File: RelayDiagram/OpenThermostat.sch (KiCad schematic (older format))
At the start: 90 parts, among them J1 Conn_01x08_Female, J2 Conn_01x15_Female, J3 Conn_01x15_Female, J4 Conn_01x09_Female, Q1 Q_NMOS_DGS, Q10 Q_NMOS_DGS, Q11 Q_NMOS_DGS, Q12 Q_NMOS_DGS, Q2 Q_NMOS_DGS, Q3 Q_NMOS_DGS, Q4 Q_NMOS_DGS, Q5 Q_NMOS_DGS, Q6 Q_NMOS_DGS, Q7 Q_NMOS_DGS, Q8 Q_NMOS_DGS, Q9 Q_NMOS_DGS, SW2 SW_Push, SW3 SW_Push, SW4 SW_Push, SW5 SW_Push, SW6 SW_Push, U1 PCF8574, U10 MB10S-13, U11 L7805CV, U2 LCD, U3 DHT11, U4 EE2-3TNU-L_DPDT_Relay, U5 EE2-3TNU-L_DPDT_Relay, U6 EE2-3TNU-L_DPDT_Relay, U7 EE2-3TNU-L_DPDT_Relay, U8 EE2-3TNU-L_DPDT_Relay, U9 EE2-3TNU-L_DPDT_Relay

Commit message: Major routing. Board should be nearly complete apart from review and minor changes.
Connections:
- wire segments 399 -> 463
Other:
- moved on the sheet: J4

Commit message: added mounting holes and power indicator LED
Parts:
- added D13: LED, Diodes_SMD:D_0805, symbol Device:LED
- added R46: 100, Resistors_SMD:R_0805, symbol Device:R
- C1: symbol solarcar-device:Capacitor_Unpolarized -> OpenThermostat-rescue:Capacitor_Unpolarized-solarcar-device
- J1: footprint Pin_Headers:Pin_Header_Angled_1x08_Pitch2.54mm -> Pin_Headers:Pin_Header_Angled_1x03_Pitch1.27mm
- J2: footprint Pin_Headers:Pin_Header_Straight_1x15_Pitch2.54mm -> Pin_Headers:Pin_Header_Straight_1x13_Pitch2.54mm_SMD_Pin1Right
- U10: symbol OpenThermostat-rescue:MB10S-13 -> OpenThermostat-rescue:MB10S-13-OpenThermostat-rescue
- U11: symbol OpenThermostat-rescue:L7805CV -> OpenThermostat-rescue:L7805CV-OpenThermostat-rescue
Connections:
- wire segments 463 -> 466
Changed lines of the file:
@@
 F 0 "J2" H 2900 2600 50  0000 L CNN
 F 1 "Conn_01x15_Female" H 2225 2525 50  0000 L CNN
-F 2 "Pin_Headers:Pin_Header_Straight_1x15_Pitch2.54mm" H 2950 3425 50  0001 C CNN
+F 2 "Pin_Headers:Pin_Header_Straight_1x13_Pitch2.54mm_SMD_Pin1Right" H 2950 3425 50  0001 C CNN
 F 3 "~" H 2950 3425 50  0001 C CNN
 	1    2950 3425
@@
 F 0 "J1" V 2100 655 50  0000 C CNN
 F 1 "Conn_01x08_Female" V 2009 655 50  0000 C CNN
-F 2 "Pin_Headers:Pin_Header_Angled_1x08_Pitch2.54mm" H 1935 725 50  0001 C CNN
+F 2 "Pin_Headers:Pin_Header_Angled_1x03_Pitch1.27mm" H 1935 725 50  0001 C CNN
 F 3 "~" H 1935 725 50  0001 C CNN
 	1    1935 725
@@
 $EndComp
 $Comp
-L OpenThermostat-rescue:MB10S-13 U10
+L OpenThermostat-rescue:MB10S-13-OpenThermostat-rescue U10
 U 1 1 5C64C7AA
 P 10975 2675
@@
 R
 $Comp
-L OpenThermostat-rescue:L7805CV U11
+L OpenThermostat-rescue:L7805CV-OpenThermostat-rescue U11
 U 1 1 5C651BD2
 P 10975 3425
@@
 $EndComp
 $Comp
-L solarcar-device:Capacitor_Unpolarized C1
+L OpenThermostat-rescue:Capacitor_Unpolarized-solarcar-device C1
 U 1 1 5C65344A
 P 11450 2675
@@
 Wire Wire Line
 	4725 3825 3950 3825
+$Comp
+L Device:LED D13
+U 1 1 5C7ACEAE
+P 2060 7800
+F 0 "D13" H 2052 7545 50  0000 C CNN
+F 1 "LED" H 2052 7636 50  0000 C CNN
+F 2 "Diodes_SMD:D_0805" H 2060 7800 50  0001 C CNN
+F 3 "~" H 2060 7800 50  0001 C CNN
+	1    2060 7800
+	-1   0    0    1
+$EndComp
+$Comp
+L Device:R R46
+U 1 1 5C7AD1B1
+P 2465 7800
+F 0 "R46" V 2340 7805 50  0000 C CNN
+F 1 "100" V 2465 7805 50  0000 C CNN
+F 2 "Resistors_SMD:R_0805" V 2395 7800 50  0001 C CNN
+F 3 "~" H 2465 7800 50  0001 C CNN
+	1    2465 7800
+	0    1    1    0
+$EndComp
+Wire Wire Line
+	2210 7800 2315 7800
+Wire Wire Line
+	2615 7800 2655 7800
+Wire Wire Line
+	1910 7800 1890 7800
+$Comp
+L power:+5V #PWR0101
+U 1 1 5C851227
+P 1890 7800
+F 0 "#PWR0101" H 1890 7650 50  0001 C CNN
+F 1 "+5V" V 1905 7928 50  0000 L CNN
+F 2 "" H 1890 7800 50  0001 C CNN
+F 3 "" H 1890 7800 50  0001 C CNN
+	1    1890 7800
+	0    -1   -1   0
+$EndComp
+$Comp
+L power:GND #PWR0102
+U 1 1 5C851537
+P 2655 7800
+F 0 "#PWR0102" H 2655 7550 50  0001 C CNN
+F 1 "GND" V 2660 7672 50  0000 R CNN
+F 2 "" H 2655 7800 50  0001 C CNN
+F 3 "" H 2655 7800 50  0001 C CNN
+	1    2655 7800
+	0    -1   -1   0
+$EndComp
 $EndSCHEMATC

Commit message: Changed to big boy header and added great logo
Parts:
- added C2, C3: 10uF, solarcar-device:Capacitor_0805, symbol OpenThermostat-rescue:Capacitor_Unpolarized-solarcar-device-OpenThermostat-resc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
- C1: symbol OpenThermostat-rescue:Capacitor_Unpolarized-solarcar-device -> OpenThermostat-rescue:Capacitor_Unpolarized-solarcar-device-OpenThermostat-rescue
- J4: footprint Pin_Headers:Pin_Header_Straight_1x09_Pitch2.54mm -> SeniorDesign:5mmPtichBlockHeader
- U10: symbol OpenThermostat-rescue:MB10S-13-OpenThermostat-rescue -> OpenThermostat-rescue:MB10S-13-OpenThermostat-rescue-OpenThermostat-rescue
- U11: symbol OpenThermostat-rescue:L7805CV-OpenThermostat-rescue -> OpenThermostat-rescue:L7805CV-OpenThermostat-rescue-OpenThermostat-rescue
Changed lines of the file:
@@
 F 0 "J4" H 10400 5900 50  0000 L CNN
 F 1 "Conn_01x09_Female" H 10400 5825 50  0000 L CNN
-F 2 "Pin_Headers:Pin_Header_Straight_1x09_Pitch2.54mm" H 10575 5325 50  0001 C CNN
+F 2 "SeniorDesign:5mmPtichBlockHeader" H 10575 5325 50  0001 C CNN
 F 3 "~" H 10575 5325 50  0001 C CNN
 	1    10575 5325
@@
 $EndComp
 $Comp
-L OpenThermostat-rescue:MB10S-13-OpenThermostat-rescue U10
+L OpenThermostat-rescue:MB10S-13-OpenThermostat-rescue-OpenThermostat-rescue U10
 U 1 1 5C64C7AA
 P 10975 2675
@@
 R
 $Comp
-L OpenThermostat-rescue:L7805CV-OpenThermostat-rescue U11
+L OpenThermostat-rescue:L7805CV-OpenThermostat-rescue-OpenThermostat-rescue U11
 U 1 1 5C651BD2
 P 10975 3425
@@
 $EndComp
 $Comp
-L OpenThermostat-rescue:Capacitor_Unpolarized-solarcar-device C1
+L OpenThermostat-rescue:Capacitor_Unpolarized-solarcar-device-OpenThermostat-rescue C1
 U 1 1 5C65344A
 P 11450 2675
@@
 	0    -1   -1   0
 $EndComp
+$Comp
+L OpenThermostat-rescue:Capacitor_Unpolarized-solarcar-device-OpenThermostat-rescue C3
+U 1 1 5C778E29
+P 3950 2575
+F 0 "C3" H 3975 2675 59  0000 L CNN
+F 1 "10uF" H 4000 2475 59  0000 L CNN
+F 2 "solarcar-device:Capacitor_0805" H 3050 3425 50  0001 C CNN
+F 3 "" H 3950 2575 50  0001 C CNN
+	1    3950 2575
+	1    0    0    -1
+$EndComp
+Connection ~ 3950 2725
+$Comp
+L power:GND #PWR0103
+U 1 1 5C7795E4
+P 3950 2425
+F 0 "#PWR0103" H 3950 2175 50  0001 C CNN
+F 1 "GND" H 3955 2252 50  0000 C CNN
+F 2 "" H 3950 2425 50  0001 C CNN
+F 3 "" H 3950 2425 50  0001 C CNN
+	1    3950 2425
+	0    1    1    0
+$EndComp
+$Comp
+L OpenThermostat-rescue:Capacitor_Unpolarized-solarcar-device-OpenThermostat-rescue C2
+U 1 1 5C77A8FC
+P 1635 4740
+F 0 "C2" H 1660 4840 59  0000 L CNN
+F 1 "10uF" H 1685 4640 59  0000 L CNN
+F 2 "solarcar-device:Capacitor_0805" H 735 5590 50  0001 C CNN
+F 3 "" H 1635 4740 50  0001 C CNN
+	1    1635 4740
+	1    0    0    -1
+$EndComp
+Connection ~ 1635 4890
+$Comp
+L power:GND #PWR0104
+U 1 1 5C77BDF8
+P 1635 4590
+F 0 "#PWR0104" H 1635 4340 50  0001 C CNN
+F 1 "GND" V 1640 4462 50  0000 R CNN
+F 2 "" H 1635 4590 50  0001 C CNN
+F 3 "" H 1635 4590 50  0001 C CNN
+	1    1635 4590
+	0    1    1    0
+$EndComp
 $EndSCHEMATC

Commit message: changed ports on micro controller to get input only ports connected to switches
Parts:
- C1, C2, C3: symbol OpenThermostat-rescue:Capacitor_Unpolarized-solarcar-device-OpenThermostat-rescue -> OpenThermostat-rescue:Capacitor_Unpolarized-solarcar-device-OpenThermostat-rescue-OpenThermostat-rescue
- U10: symbol OpenThermostat-rescue:MB10S-13-OpenThermostat-rescue-OpenThermostat-rescue -> OpenThermostat-rescue:MB10S-13-OpenThermostat-rescue-OpenThermostat-rescue-OpenThermostat-rescue
- U11: symbol OpenThermostat-rescue:L7805CV-OpenThermostat-rescue-OpenThermostat-rescue -> OpenThermostat-rescue:L7805CV-OpenThermostat-rescue-OpenThermostat-rescue-OpenThermostat-rescue
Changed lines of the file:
@@
 $EndComp
 $Comp
-L OpenThermostat-rescue:MB10S-13-OpenThermostat-rescue-OpenThermostat-rescue U10
+L OpenThermostat-rescue:MB10S-13-OpenThermostat-rescue-OpenThermostat-rescue-OpenThermostat-rescue U10
 U 1 1 5C64C7AA
 P 10975 2675
@@
 R
 $Comp
-L OpenThermostat-rescue:L7805CV-OpenThermostat-rescue-OpenThermostat-rescue U11
+L OpenThermostat-rescue:L7805CV-OpenThermostat-rescue-OpenThermostat-rescue-OpenThermostat-rescue U11
 U 1 1 5C651BD2
 P 10975 3425
@@
 $EndComp
 $Comp
-L OpenThermostat-rescue:Capacitor_Unpolarized-solarcar-device-OpenThermostat-rescue C1
+L OpenThermostat-rescue:Capacitor_Unpolarized-solarcar-device-OpenThermostat-rescue-OpenThermostat-rescue C1
 U 1 1 5C65344A
 P 11450 2675
@@
 	1655 3925 1655 4565
 Wire Wire Line
-	1655 4565 4110 4565
-Wire Wire Line
 	2750 4125 1735 4125
 Wire Wire Line
 	1735 4125 1735 4515
-Wire Wire Line
-	1735 4515 4225 4515
 Wire Wire Line
 	6375 900  6400 900
@@
 	6075 9950 4725 9950
 Wire Wire Line
-	4725 9950 4725 3825
-Wire Wire Line
 	6075 9125 4825 9125
-Wire Wire Line
-	4825 9125 4825 3725
 Wire Wire Line
 	6075 8325 4925 8325
@@
 Wire Wire Line
 	3990 4640 3990 6040
-Wire Wire Line
-	4110 4565 4110 6040
-Wire Wire Line
-	4225 4515 4225 6040
 Wire Wire Line
 	8400 8800 8425 8800
@@
 Wire Wire Line
 	4925 3625 3950 3625
-Wire Wire Line
-	4825 3725 3950 3725
-Wire Wire Line
-	4725 3825 3950 3825
 $Comp
 L Device:LED D13
@@
 $EndComp
 $Comp
-L OpenThermostat-rescue:Capacitor_Unpolarized-solarcar-device-OpenThermostat-rescue C3
+L OpenThermostat-rescue:Capacitor_Unpolarized-solarcar-device-OpenThermostat-rescue-OpenThermostat-rescue C3
 U 1 1 5C778E29
 P 3950 2575
@@
 $EndComp
 $Comp
-L OpenThermostat-rescue:Capacitor_Unpolarized-solarcar-device-OpenThermostat-rescue C2
+L OpenThermostat-rescue:Capacitor_Unpolarized-solarcar-device-OpenThermostat-rescue-OpenThermostat-rescue C2
 U 1 1 5C77A8FC
 P 1635 4740
@@
 	0    1    1    0
 $EndComp
+Wire Wire Line
+	4825 4515 4825 9125
+Wire Wire Line
+	1735 4515 4825 4515
+Wire Wire Line
+	4725 4565 4725 9950
+Wire Wire Line
+	1655 4565 4725 4565
+Wire Wire Line
+	4110 6040 4110 3825
+Wire Wire Line
+	4110 3825 3950 3825
+Wire Wire Line
+	3950 3725 4225 3725
+Wire Wire Line
+	4225 3725 4225 6040
 $EndSCHEMATC

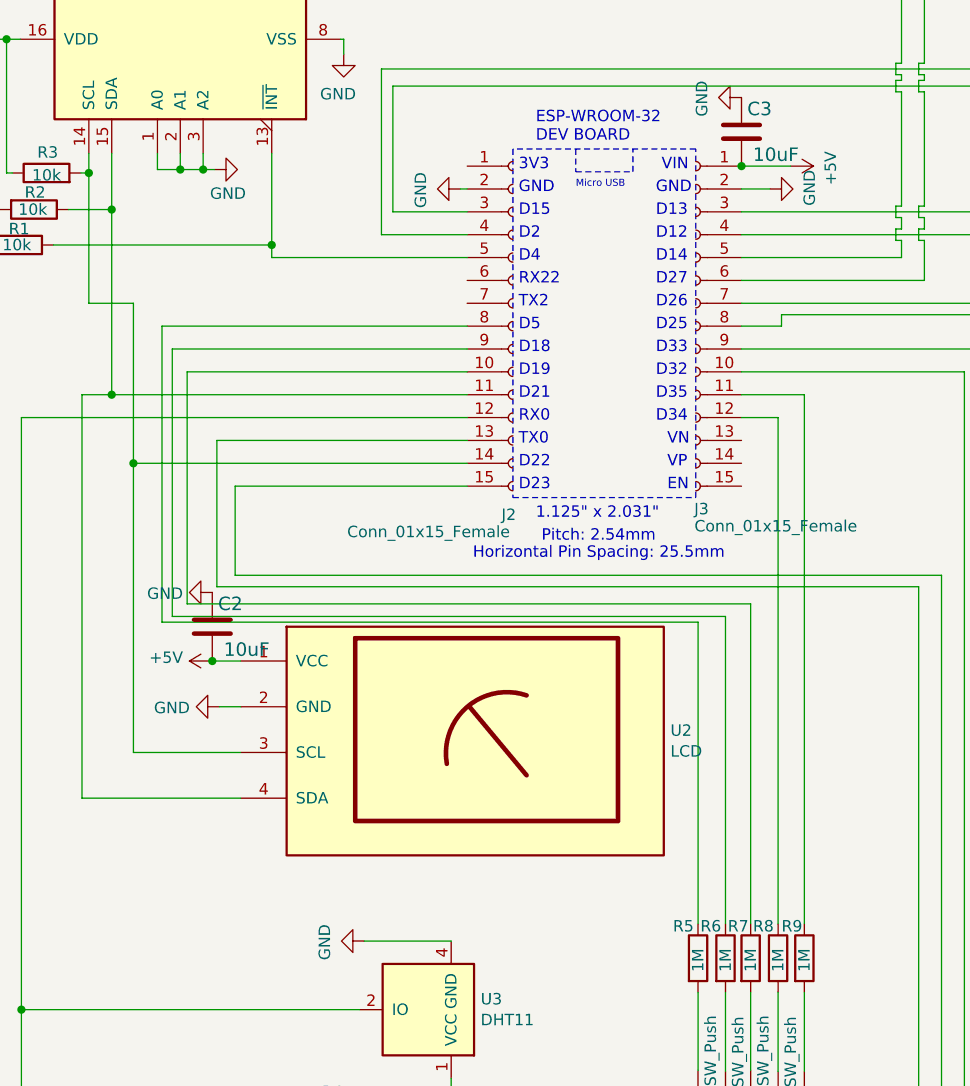
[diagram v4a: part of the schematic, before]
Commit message: Added pull up resistors
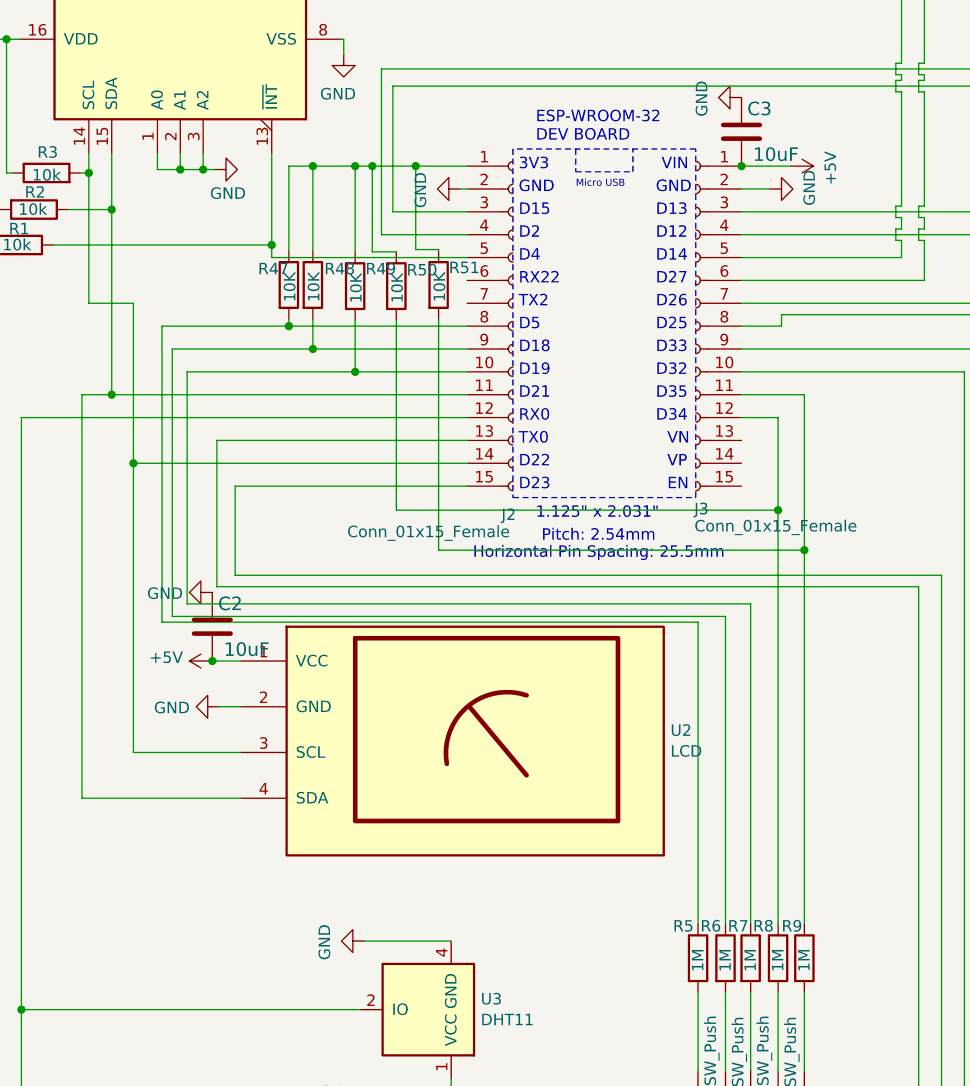
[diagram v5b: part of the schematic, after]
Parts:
- added R47, R48, R49, R50, R51: 10K, Resistors_SMD:R_0805, symbol Device:R
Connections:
- net at J2.1 (Pin_1): now also R47.1, R48.1, R49.1, R50.1, R51.1
- net at J2.10 (Pin_10), R7.1: now also R49.2
- net at J2.8 (Pin_8), R5.1: now also R47.2
- net at J2.9 (Pin_9), R6.1: now also R48.2
- net at J3.11 (Pin_11), R9.1: now also R51.2
- net at J3.12 (Pin_12), R8.1: now also R50.2
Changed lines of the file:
@@
 	1415 4720 3760 4720
 Wire Wire Line
-	1415 3425 2750 3425
+	1415 3425 1970 3425
 Wire Wire Line
 	1460 3525 1460 4695
@@
 	1460 4695 3880 4695
 Wire Wire Line
-	1460 3525 2750 3525
+	1460 3525 2075 3525
 Wire Wire Line
 	1525 3625 1525 4640
@@
 	1525 4640 3990 4640
 Wire Wire Line
-	1525 3625 2750 3625
+	1525 3625 2260 3625
 Wire Wire Line
 	2750 3925 1655 3925
@@
 	1655 4565 4725 4565
 Wire Wire Line
-	4110 6040 4110 3825
+	4110 6040 4110 4230
 Wire Wire Line
 	4110 3825 3950 3825
@@
 	3950 3725 4225 3725
 Wire Wire Line
-	4225 3725 4225 6040
+	4225 3725 4225 4405
+$Comp
+L Device:R R47
+U 1 1 5CC14F48
+P 1970 3245
+F 0 "R47" H 1835 3315 50  0000 L CNN
+F 1 "10K" V 1975 3170 50  0000 L CNN
+F 2 "Resistors_SMD:R_0805" V 1900 3245 50  0001 C CNN
+F 3 "~" H 1970 3245 50  0001 C CNN
+	1    1970 3245
+	1    0    0    -1
+$EndComp
+$Comp
+L Device:R R48
+U 1 1 5CC154F4
+P 2075 3245
+F 0 "R48" H 2125 3315 50  0000 L CNN
+F 1 "10K" V 2080 3170 50  0000 L CNN
+F 2 "Resistors_SMD:R_0805" V 2005 3245 50  0001 C CNN
+F 3 "~" H 2075 3245 50  0001 C CNN
+	1    2075 3245
+	1    0    0    -1
+$EndComp
+$Comp
+L Device:R R49
+U 1 1 5CC4CAE2
+P 2260 3250
+F 0 "R49" H 2305 3325 50  0000 L CNN
+F 1 "10K" V 2265 3175 50  0000 L CNN
+F 2 "Resistors_SMD:R_0805" V 2190 3250 50  0001 C CNN
+F 3 "~" H 2260 3250 50  0001 C CNN
+	1    2260 3250
+	1    0    0    -1
+$EndComp
+$Comp
+L Device:R R50
+U 1 1 5CC840C3
+P 2440 3250
+F 0 "R50" H 2485 3320 50  0000 L CNN
+F 1 "10K" V 2445 3175 50  0000 L CNN
+F 2 "Resistors_SMD:R_0805" V 2370 3250 50  0001 C CNN
+F 3 "~" H 2440 3250 50  0001 C CNN
+	1    2440 3250
+	1    0    0    -1
+$EndComp
+$Comp
+L Device:R R51
+U 1 1 5CCBB6B7
+P 2625 3245
+F 0 "R51" H 2670 3320 50  0000 L CNN
+F 1 "10K" V 2630 3170 50  0000 L CNN
+F 2 "Resistors_SMD:R_0805" V 2555 3245 50  0001 C CNN
+F 3 "~" H 2625 3245 50  0001 C CNN
+	1    2625 3245
+	1    0    0    -1
+$EndComp
+Wire Wire Line
+	1970 2725 1970 3095
+Wire Wire Line
+	2075 3095 2075 2725
+Connection ~ 2075 2725
+Wire Wire Line
+	2075 2725 1970 2725
+Wire Wire Line
+	2260 3100 2260 2725
+Connection ~ 2260 2725
+Wire Wire Line
+	2260 2725 2075 2725
+Wire Wire Line
+	2440 3100 2335 3100
+Wire Wire Line
+	2335 3100 2335 2725
+Connection ~ 2335 2725
+Wire Wire Line
+	2335 2725 2260 2725
+Wire Wire Line
+	2625 3090 2525 3090
+Wire Wire Line
+	2525 3090 2525 2725
+Wire Wire Line
+	2525 2725 2335 2725
+Wire Wire Line
+	2625 3095 2625 3090
+Wire Wire Line
+	1970 3395 1970 3425
+Connection ~ 1970 3425
+Wire Wire Line
+	1970 3425 2750 3425
+Wire Wire Line
+	2075 3395 2075 3525
+Connection ~ 2075 3525
+Wire Wire Line
+	2075 3525 2750 3525
+Wire Wire Line
+	2260 3400 2260 3625
+Connection ~ 2260 3625
+Wire Wire Line
+	2260 3625 2750 3625
+Wire Wire Line
+	2440 3400 2440 4230
+Wire Wire Line
+	2440 4230 4110 4230
+Connection ~ 4110 4230
+Wire Wire Line
+	4110 4230 4110 3825
+Wire Wire Line
+	2625 4405 4225 4405
+Wire Wire Line
+	2625 3395 2625 4405
+Connection ~ 4225 4405
+Wire Wire Line
+	4225 4405 4225 6040
+Connection ~ 2525 2725
+Wire Wire Line
+	2750 2725 2525 2725
 $EndSCHEMATC
